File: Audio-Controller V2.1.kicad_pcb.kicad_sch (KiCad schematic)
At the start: 16 parts

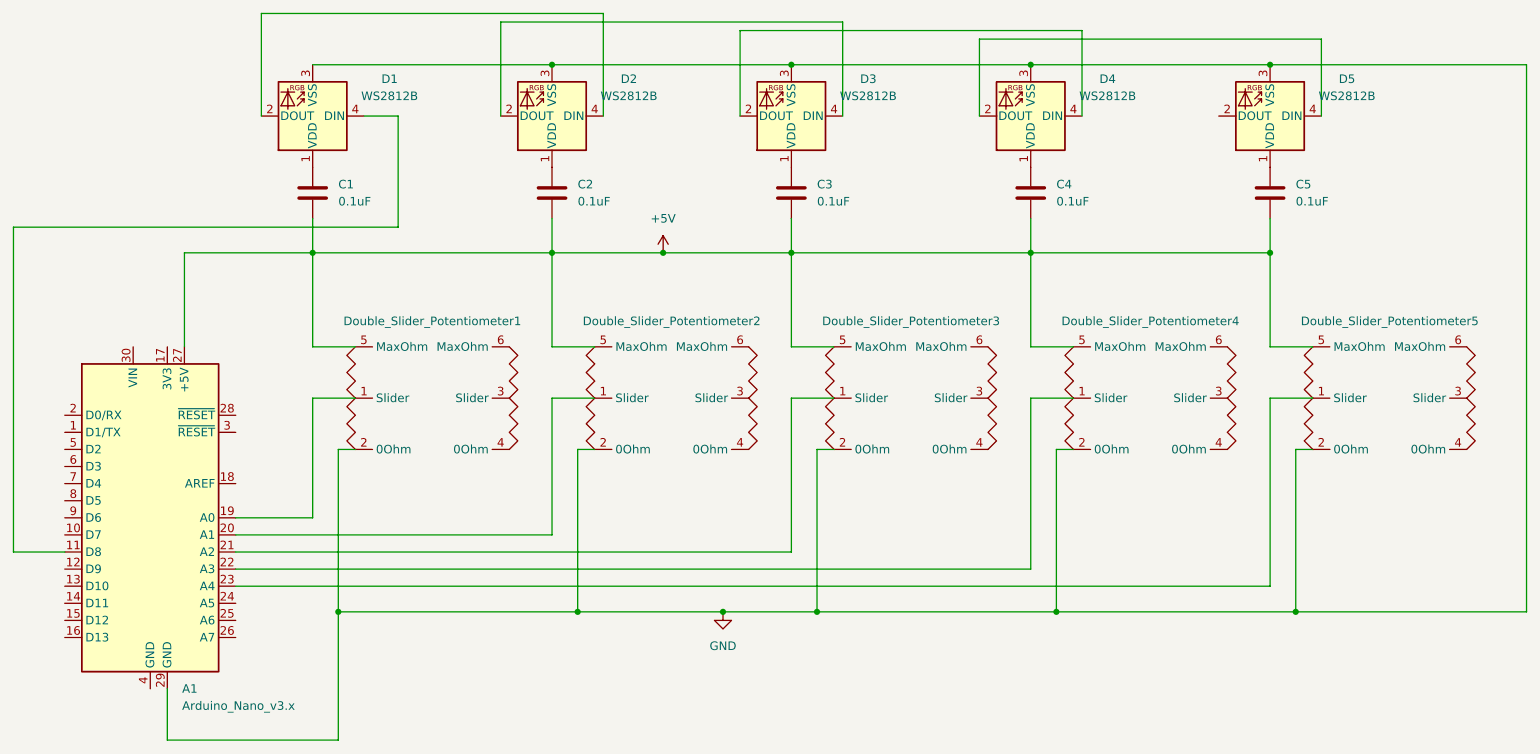
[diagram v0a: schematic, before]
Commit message: Version 2.1
Fixed errors and tested design.
Working code included.
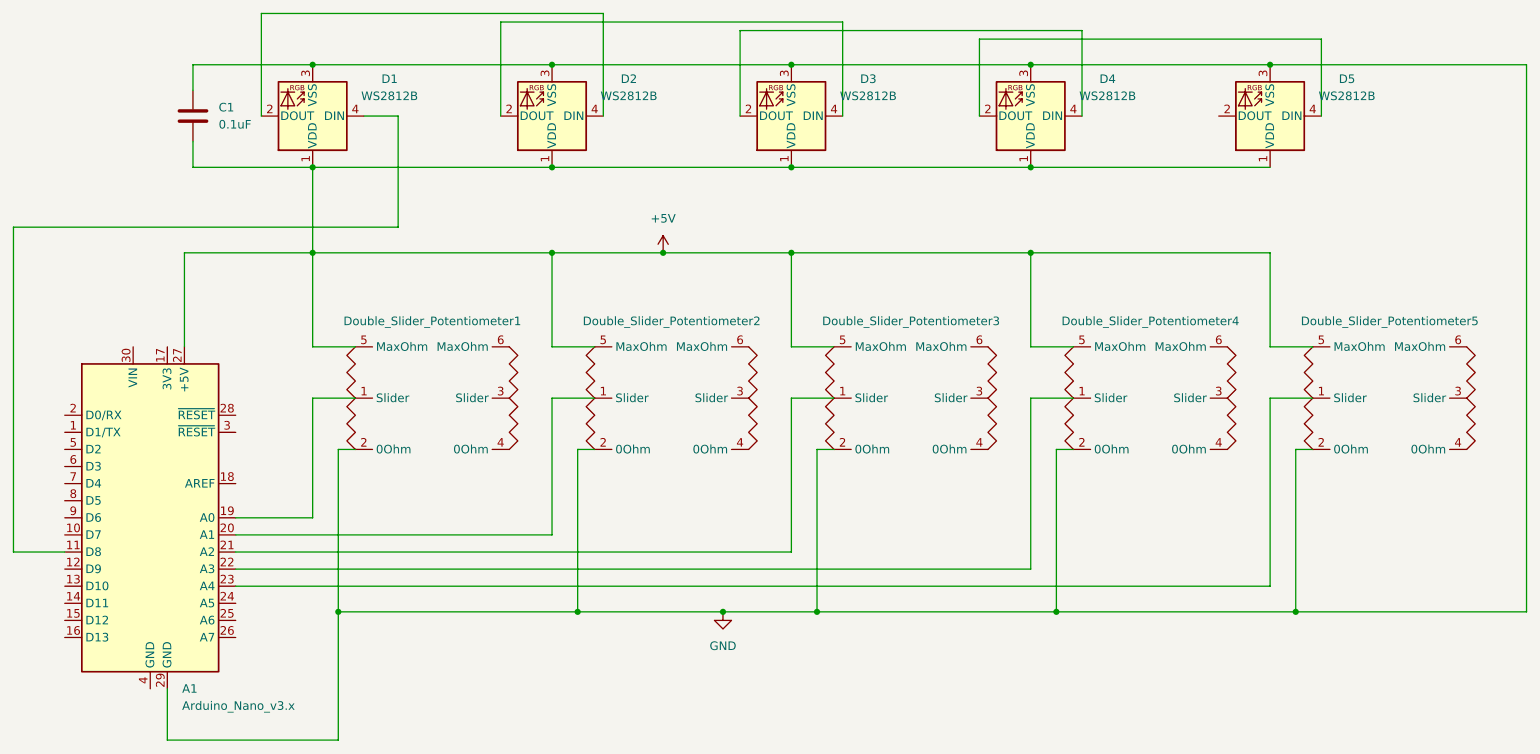
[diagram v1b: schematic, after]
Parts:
- removed C2, C3, C4, C5: 0.1uF, Capacitor_SMD:C_0805_2012Metric_Pad1.18x1.45mm_HandSolder, symbol Device:C
- C1: footprint Capacitor_SMD:C_0805_2012Metric_Pad1.18x1.45mm_HandSolder -> Capacitor_SMD:C_1206_3216Metric_Pad1.33x1.80mm_HandSolder
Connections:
- net +5V: now also D1.1 (VDD), D2.1 (VDD), D3.1 (VDD), D4.1 (VDD), D5.1 (VDD)
- net GND: now also C1.1
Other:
- moved on the sheet: C1
